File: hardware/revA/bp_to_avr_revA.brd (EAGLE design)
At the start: 21.3 x 21.6 mm, 5 parts, among them J1 CON_HEADER_2X05-PTH+SHROUDED_B

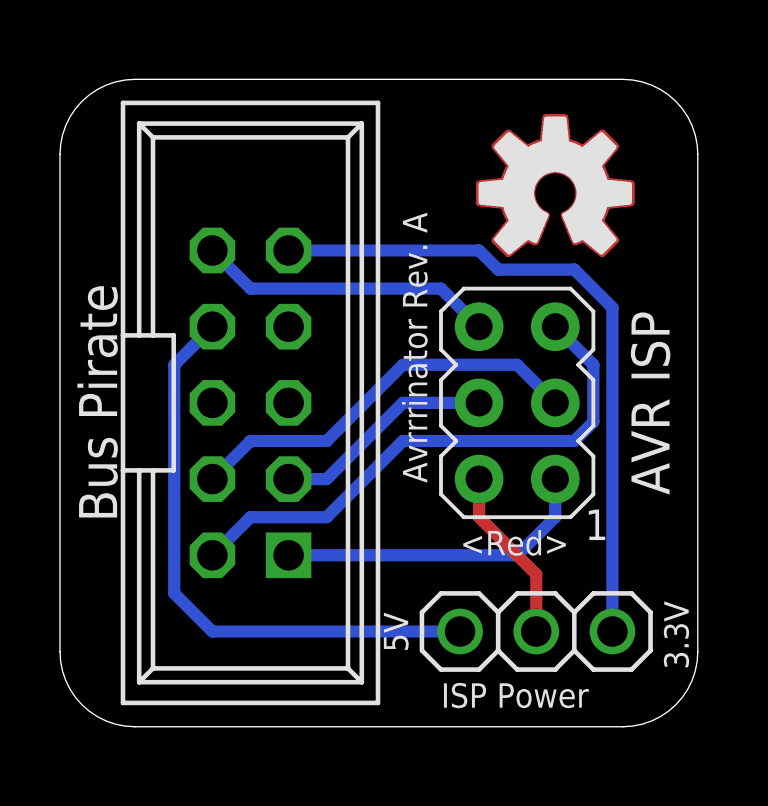
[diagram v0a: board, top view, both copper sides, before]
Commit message: Avrrrinator Rev. A cosmetic/BOM changes
- Align OSHW logo w/PCB use direction + no mask
- Has bottom alignment silk for bus pirate header underneath
- Poly pour + mask text
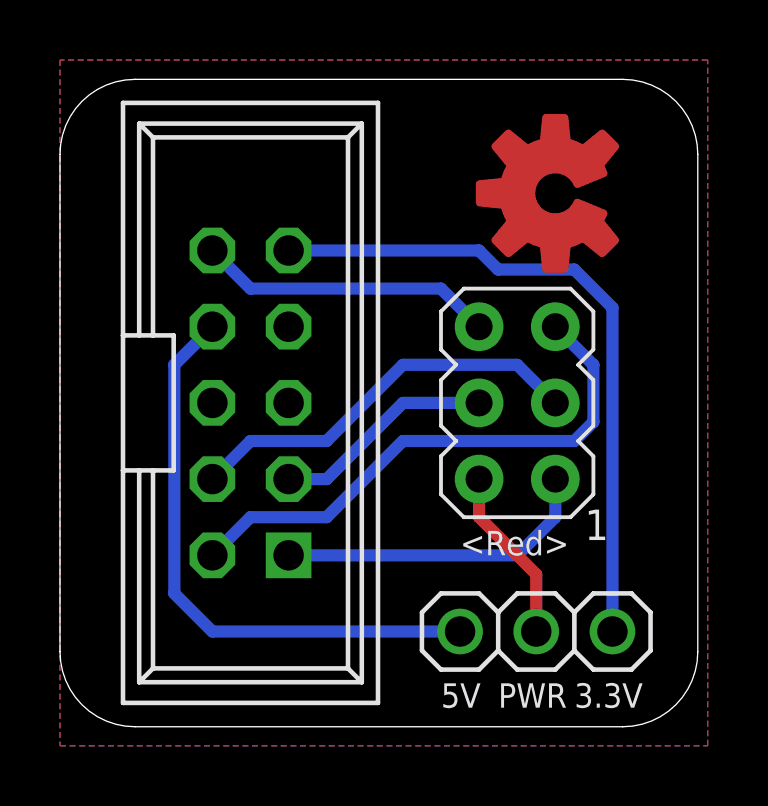
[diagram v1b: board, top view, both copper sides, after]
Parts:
- removed U$1: (no value), adafruit:OSHWLOGO_TOP_0.2
- removed U$2: (no value), SparkFun-Aesthetics:OSHW-LOGO-M
- added U$4: (no value), bp_to_avr:ADAFRUIT_OSHWLOGO_TOP_0.2_NO_MASK
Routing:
- added copper zone on layer 1, net GND
- added copper zone on layer 16, net GND
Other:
- board text added: "Bus Pirate v3"
- board text added: "Bus Pirate v3 ISP adapter 2014-2-18"
- board text added: "PWR"
- board text added: "open.konspyre.org/avra"
- board text removed: "Bus Pirate"
- board text removed: "Bus Pirate v3 to AVR ISP Adapter"
- board text removed: "ISP Power"
- board text removed: "davidk - open.konspyre.org - <1/6/13>"
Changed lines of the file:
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@@
 <wire x1="3.77" y1="0.635" x2="20.03" y2="0.635" width="0" layer="20"/>
 <wire x1="20.03" y1="0.635" x2="22.53" y2="3.135" width="0" layer="20" curve="90"/>
-<text x="2.54" y="11.43" size="1.27" layer="121" font="vector" ratio="20" rot="R270" align="center">Bus Pirate</text>
-<text x="20.955" y="11.43" size="1.27" layer="121" font="vector" ratio="20" rot="R270" align="center">AVR ISP</text>
+<text x="2.54" y="11.43" size="1.27" layer="29" font="vector" ratio="20" rot="R270" align="center">Bus Pirate v3</text>
+<text x="20.32" y="11.43" size="1.27" layer="29" font="vector" ratio="20" rot="R270" align="center">AVR ISP</text>
 <text x="14.605" y="6.35" size="0.8128" layer="121" font="vector" ratio="20">&lt;Red&gt;</text>
-<text x="12.065" y="4.445" size="0.8128" layer="121" font="vector" ratio="20" rot="R270">5V</text>
-<text x="22.225" y="2.54" size="0.8128" layer="121" font="vector" ratio="20" rot="R90">3.3V</text>
-<text x="12.7" y="17.78" size="0.8128" layer="121" font="vector" ratio="20" rot="R270">Avrrrinator Rev. A</text>
-<text x="21.59" y="20.955" size="0.6096" layer="122" font="vector" ratio="20" rot="MR0">Bus Pirate v3 to AVR ISP Adapter</text>
-<text x="13.97" y="1.27" size="0.8128" layer="121" font="vector" ratio="20">ISP Power</text>
-<text x="21.59" y="19.05" size="0.6096" layer="122" font="vector" ratio="20" rot="MR0">davidk - open.konspyre.org - &lt;1/6/13&gt;</text>
+<text x="13.97" y="1.27" size="0.8128" layer="121" font="vector" ratio="20">5V</text>
+<text x="18.415" y="1.27" size="0.8128" layer="121" font="vector" ratio="20">3.3V</text>
+<text x="12.7" y="20.32" size="1.016" layer="29" font="vector" ratio="20" rot="R270">Avrrrinator Rev. A</text>
+<text x="20.32" y="17.145" size="1.016" layer="30" font="vector" ratio="20" rot="MR0">Bus Pirate v3 ISP
+adapter
+2014-2-18</text>
+<text x="15.875" y="1.27" size="0.8128" layer="121" font="vector" ratio="20">PWR</text>
+<text x="20.955" y="5.08" size="0.6096" layer="30" ratio="20" rot="MR90">open.konspyre.org/avra</text>
+<wire x1="4.445" y1="2.54" x2="4.445" y2="8.89" width="0.4064" layer="122"/>
+<wire x1="4.445" y1="20.32" x2="4.445" y2="13.97" width="0.4064" layer="122"/>
+<rectangle x1="3.175" y1="8.89" x2="5.08" y2="13.97" layer="122"/>
 </plain>
 <attributes>
@@
 <attribute name="VALUE" x="13.335" y="0.635" size="1.27" layer="27"/>
 </element>
-<element name="U$1" library="adafruit" package="OSHWLOGO_TOP_0.2" value="" x="17.78" y="18.415"/>
-<element name="U$2" library="SparkFun-Aesthetics" package="OSHW-LOGO-M" value="" x="17.78" y="18.415"/>
+<element name="U$4" library="bp_to_avr" package="ADAFRUIT_OSHWLOGO_TOP_0.2_NO_MASK" value="" x="17.78" y="18.415" rot="R90"/>
 </elements>
 <signals>
@@
 <wire x1="7.62" y1="15.24" x2="13.97" y2="15.24" width="0.4064" layer="16"/>
 <wire x1="13.97" y1="15.24" x2="15.24" y2="13.97" width="0.4064" layer="16"/>
+<polygon width="0.4064" layer="1" isolate="0.3048">
+<vertex x="1.27" y="22.86"/>
+<vertex x="1.27" y="0"/>
+<vertex x="22.86" y="0"/>
+<vertex x="22.86" y="22.86"/>
+</polygon>
+<polygon width="0.4064" layer="16" isolate="0.3048">
+<vertex x="1.27" y="22.86"/>
+<vertex x="1.27" y="0"/>
+<vertex x="22.86" y="0"/>
+<vertex x="22.86" y="22.86"/>
+</polygon>
 </signal>
 </signals>
 </board>
 </drawing>
+<compatibility>
+<note version="6.3" minversion="6.2.2" severity="warning">
+Since Version 6.2.2 text objects can contain more than one line,
+which will not be processed correctly with this version.
+</note>
+</compatibility>
 </eagle>
